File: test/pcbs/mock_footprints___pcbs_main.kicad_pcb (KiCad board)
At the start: 2 copper layers, 19 x 19 mm, 4 parts

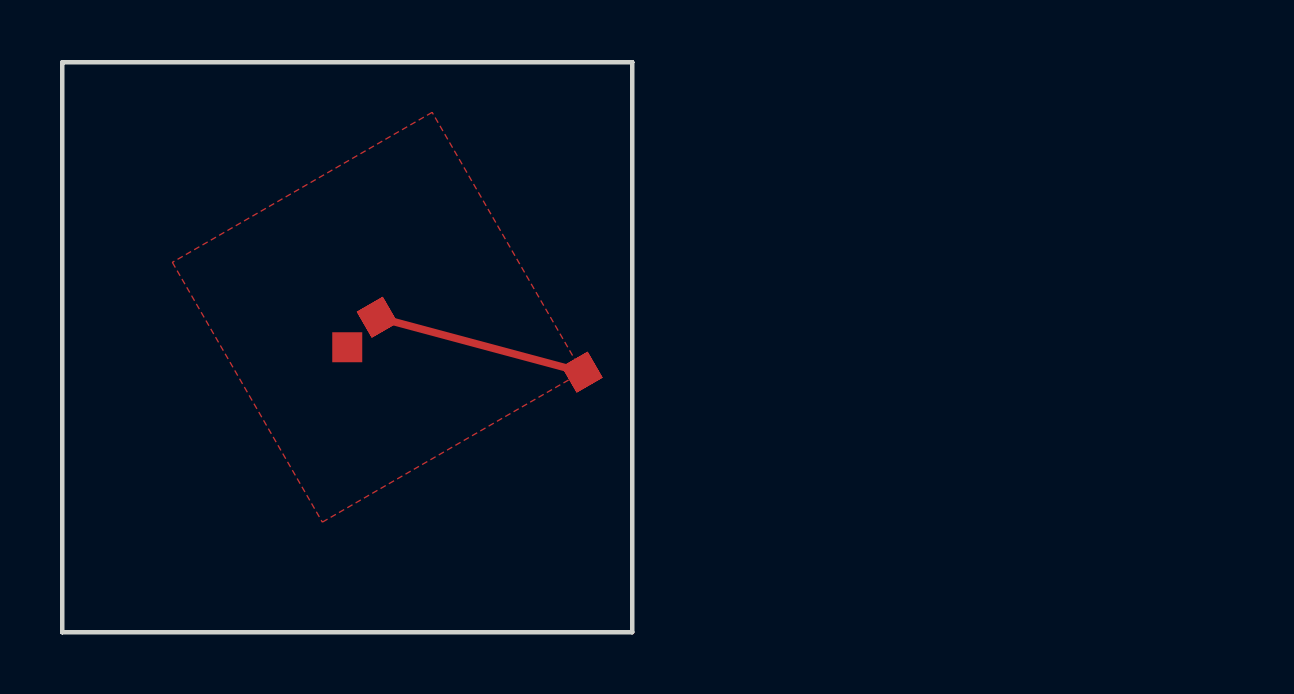
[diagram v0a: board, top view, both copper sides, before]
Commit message: Per-footprint mirror overrides, better coordinate support
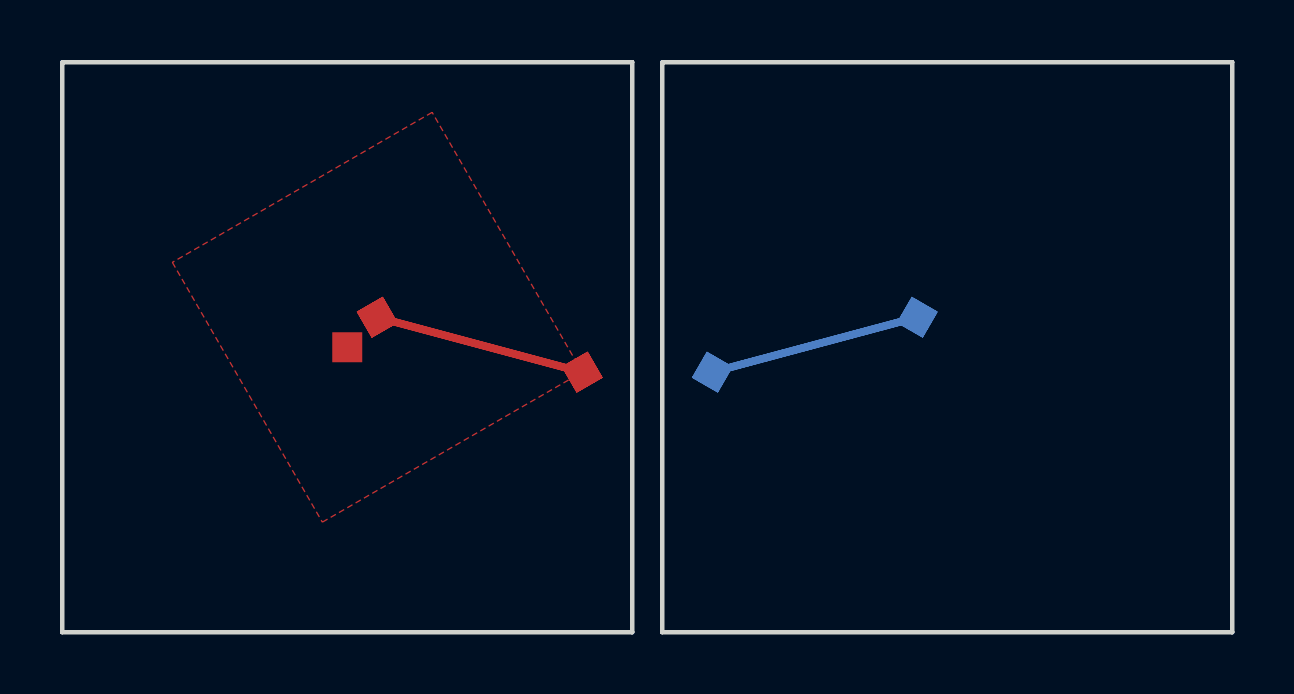
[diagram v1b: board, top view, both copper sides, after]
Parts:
- removed the ? at (1.00, -1.00)
- added ? (x2): , trace_test, F.Cu at (1.00, -1.00)
- added ? (x2): , trace_test, B.Cu at (19.0, -1.00)
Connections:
- net T3_3 renamed T6_3
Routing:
- net P1: track 7.07 -> 28.3 mm
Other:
- board size 19 x 19 mm -> 39 x 19 mm
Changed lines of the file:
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@@
             (net 0 "")
 (net 1 "P1")
-(net 2 "T3_1")
-(net 3 "T3_2")
-(net 4 "T3_3")
+(net 2 "T6_1")
+(net 3 "T6_2")
+(net 4 "T6_3")
   (net_class Default "This is the default net class."
     (clearance 0.2)
@@
     (add_net "")
 (add_net "P1")
-(add_net "T3_1")
-(add_net "T3_2")
-(add_net "T3_3")
+(add_net "T6_1")
+(add_net "T6_2")
+(add_net "T6_3")
   )
+                (module trace_test (layer F.Cu)
+                    (at 1 -1 30)
+                    (pad 1 smd rect (at 0 0 30) (size 1 1) (layers F.Cu F.Paste F.Mask)
+                        (net 1 "P1") (solder_mask_margin 0.2))
+                    (pad 2 smd rect (at 5 5 30) (size 1 1) (layers F.Cu F.Paste F.Mask)
+                        (net 1 "P1") (solder_mask_margin 0.2))
+                )
+                (segment (start 1 -1) (end 7.830127 0.8301270000000001) (width 0.25) (layer F.Cu) (net 1))
+                (module trace_test (layer B.Cu)
+                    (at 19 -1 -30)
+                    (pad 1 smd rect (at 0 0 -30) (size 1 1) (layers B.Cu B.Paste B.Mask)
+                        (net 1 "P1") (solder_mask_margin 0.2))
+                    (pad 2 smd rect (at -5 5 -30) (size 1 1) (layers B.Cu B.Paste B.Mask)
+                        (net 1 "P1") (solder_mask_margin 0.2))
+                )
+                (segment (start 19 -1) (end 12.169872999999999 0.8301270000000001) (width 0.25) (layer B.Cu) (net 1))
+                (module trace_test (layer B.Cu)
+                    (at 19 -1 -30)
+                    (pad 1 smd rect (at 0 0 -30) (size 1 1) (layers B.Cu B.Paste B.Mask)
+                        (net 1 "P1") (solder_mask_margin 0.2))
+                    (pad 2 smd rect (at -5 5 -30) (size 1 1) (layers B.Cu B.Paste B.Mask)
+                        (net 1 "P1") (solder_mask_margin 0.2))
+                )
+                (segment (start 19 -1) (end 12.169872999999999 0.8301270000000001) (width 0.25) (layer B.Cu) (net 1))
                 (module trace_test (layer F.Cu)
                     (at 1 -1 30)
@@
                     (at 0 0 0)
                     (pad 1 smd rect (at 0 0 0) (size 1 1) (layers F.Cu F.Paste F.Mask)
-                        (net 2 "T3_1") (solder_mask_margin 0.2))
+                        (net 2 "T6_1") (solder_mask_margin 0.2))
                     (pad 1 smd rect (at 0 0 0) (size 1 1) (layers F.Cu F.Paste F.Mask)
-                        (net 3 "T3_2") (solder_mask_margin 0.2))
+                        (net 3 "T6_2") (solder_mask_margin 0.2))
                     (pad 1 smd rect (at 0 0 0) (size 1 1) (layers F.Cu F.Paste F.Mask)
-                        (net 4 "T3_3") (solder_mask_margin 0.2))
+                        (net 4 "T6_3") (solder_mask_margin 0.2))
                 )
                 (module anchor_test (layer F.Cu)
@@
 (gr_line (start 9.5 -9.5) (end -9.5 -9.5) (angle 90) (layer Edge.Cuts) (width 0.15))
 (gr_line (start -9.5 -9.5) (end -9.5 9.5) (angle 90) (layer Edge.Cuts) (width 0.15))
+(gr_line (start 10.5 9.5) (end 29.5 9.5) (angle 90) (layer Edge.Cuts) (width 0.15))
+(gr_line (start 29.5 9.5) (end 29.5 -9.5) (angle 90) (layer Edge.Cuts) (width 0.15))
+(gr_line (start 29.5 -9.5) (end 10.5 -9.5) (angle 90) (layer Edge.Cuts) (width 0.15))
+(gr_line (start 10.5 -9.5) (end 10.5 9.5) (angle 90) (layer Edge.Cuts) (width 0.15))
 )

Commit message: New Kicad format plus tests
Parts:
- removed the ? at (1.00, -1.00) (x2)
- removed the ? at (19.0, -1.00) (x2)
- added ? (x2): , trace_test, F.Cu at (1.00, -1.00)
- added ? (x2): , trace_test, B.Cu at (19.0, -1.00)
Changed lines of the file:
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@@
-(kicad_pcb (version 20171130) (host pcbnew 5.1.6)
-  (page A3)
+(kicad_pcb (version 20211014) (generator pcbnew)
+  (general
+    (thickness 1.6)
+  )
+  (paper "A3")
   (title_block
     (title main)
@@
     (company Unknown)
   )
-  (general
-    (thickness 1.6)
-  )
   (layers
-    (0 F.Cu signal)
-    (31 B.Cu signal)
-    (32 B.Adhes user)
-    (33 F.Adhes user)
-    (34 B.Paste user)
-    (35 F.Paste user)
-    (36 B.SilkS user)
-    (37 F.SilkS user)
-    (38 B.Mask user)
-    (39 F.Mask user)
-    (40 Dwgs.User user)
-    (41 Cmts.User user)
-    (42 Eco1.User user)
-    (43 Eco2.User user)
-    (44 Edge.Cuts user)
-    (45 Margin user)
-    (46 B.CrtYd user)
-    (47 F.CrtYd user)
-    (48 B.Fab user)
-    (49 F.Fab user)
+    (0 "F.Cu" signal)
+    (31 "B.Cu" signal)
+    (32 "B.Adhes" user "B.Adhesive")
+    (33 "F.Adhes" user "F.Adhesive")
+    (34 "B.Paste" user)
+    (35 "F.Paste" user)
+    (36 "B.SilkS" user "B.Silkscreen")
+    (37 "F.SilkS" user "F.Silkscreen")
+    (38 "B.Mask" user)
+    (39 "F.Mask" user)
+    (40 "Dwgs.User" user "User.Drawings")
+    (41 "Cmts.User" user "User.Comments")
+    (42 "Eco1.User" user "User.Eco1")
+    (43 "Eco2.User" user "User.Eco2")
+    (44 "Edge.Cuts" user)
+    (45 "Margin" user)
+    (46 "B.CrtYd" user "B.Courtyard")
+    (47 "F.CrtYd" user "F.Courtyard")
+    (48 "B.Fab" user)
+    (49 "F.Fab" user)
   )
   (setup
@@
     (visible_elements FFFFFF7F)
     (pcbplotparams
-      (layerselection 0x010fc_ffffffff)
+      (layerselection 0x00010fc_ffffffff)
+      (disableapertmacros false)
       (usegerberextensions false)
       (usegerberattributes true)
       (usegerberadvancedattributes true)
       (creategerberjobfile true)
+      (svguseinch false)
+      (svgprecision 6)
       (excludeedgelayer true)
-      (linewidth 0.100000)
       (plotframeref false)
       (viasonmask false)
@@
       (hpglpenspeed 20)
       (hpglpendiameter 15.000000)
+      (dxfpolygonmode true)
+      (dxfimperialunits true)
+      (dxfusepcbnewfont true)
       (psnegative false)
       (psa4output false)
@@
       (plotvalue true)
       (plotinvisibletext false)
-      (padsonsilk false)
+      (sketchpadsonfab false)
       (subtractmaskfromsilk false)
       (outputformat 1)
@@
       (drillshape 1)
       (scaleselection 1)
-      (outputdirectory ""))
+      (outputdirectory "")
+    )
   )
             (net 0 "")
@@
                     (fp_line (start 0 0) (end 10 -10) (layer Dwgs.User) (width 0.05))
                 )
-            (gr_line (start -9.5 9.5) (end 9.5 9.5) (angle 90) (layer Edge.Cuts) (width 0.15))
-(gr_line (start 9.5 9.5) (end 9.5 -9.5) (angle 90) (layer Edge.Cuts) (width 0.15))
-(gr_line (start 9.5 -9.5) (end -9.5 -9.5) (angle 90) (layer Edge.Cuts) (width 0.15))
-(gr_line (start -9.5 -9.5) (end -9.5 9.5) (angle 90) (layer Edge.Cuts) (width 0.15))
-(gr_line (start 10.5 9.5) (end 29.5 9.5) (angle 90) (layer Edge.Cuts) (width 0.15))
-(gr_line (start 29.5 9.5) (end 29.5 -9.5) (angle 90) (layer Edge.Cuts) (width 0.15))
-(gr_line (start 29.5 -9.5) (end 10.5 -9.5) (angle 90) (layer Edge.Cuts) (width 0.15))
-(gr_line (start 10.5 -9.5) (end 10.5 9.5) (angle 90) (layer Edge.Cuts) (width 0.15))
+            (gr_line (start -9.5 9.5) (end 9.5 9.5) (layer "Edge.Cuts") (width 0.15))
+(gr_line (start 9.5 9.5) (end 9.5 -9.5) (layer "Edge.Cuts") (width 0.15))
+(gr_line (start 9.5 -9.5) (end -9.5 -9.5) (layer "Edge.Cuts") (width 0.15))
+(gr_line (start -9.5 -9.5) (end -9.5 9.5) (layer "Edge.Cuts") (width 0.15))
+(gr_line (start 10.5 9.5) (end 29.5 9.5) (layer "Edge.Cuts") (width 0.15))
+(gr_line (start 29.5 9.5) (end 29.5 -9.5) (layer "Edge.Cuts") (width 0.15))
+(gr_line (start 29.5 -9.5) (end 10.5 -9.5) (layer "Edge.Cuts") (width 0.15))
+(gr_line (start 10.5 -9.5) (end 10.5 9.5) (layer "Edge.Cuts") (width 0.15))
 )

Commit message: Add parenthesis to title block
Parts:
- removed the ? at (1.00, -1.00) (x2)
- removed the ? at (19.0, -1.00) (x2)
- added ? (x2): , trace_test, F.Cu at (1.00, -1.00)
- added ? (x2): , trace_test, B.Cu at (19.0, -1.00)
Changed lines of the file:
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@@
   (paper "A3")
   (title_block
-    (title main)
-    (rev v1.0.0)
-    (company Unknown)
+    (title "main")
+    (rev "v1.0.0")
+    (company "Unknown")
   )
   (layers
